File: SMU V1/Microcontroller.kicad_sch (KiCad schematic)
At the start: 0 parts

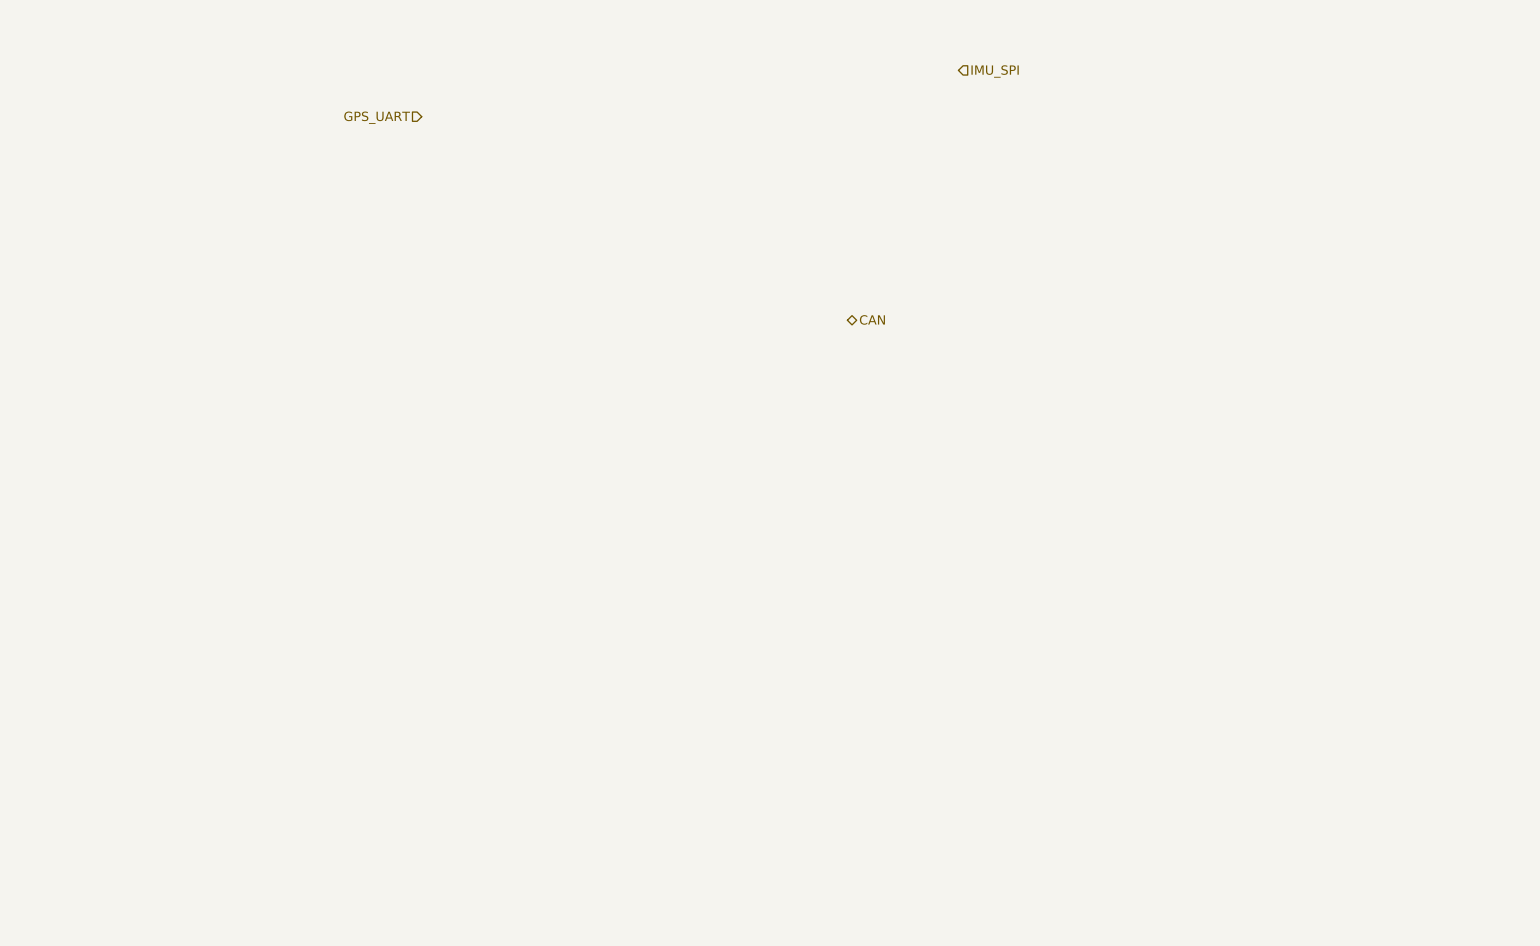
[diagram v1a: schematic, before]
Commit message: halfway done with routing, still needs antenna
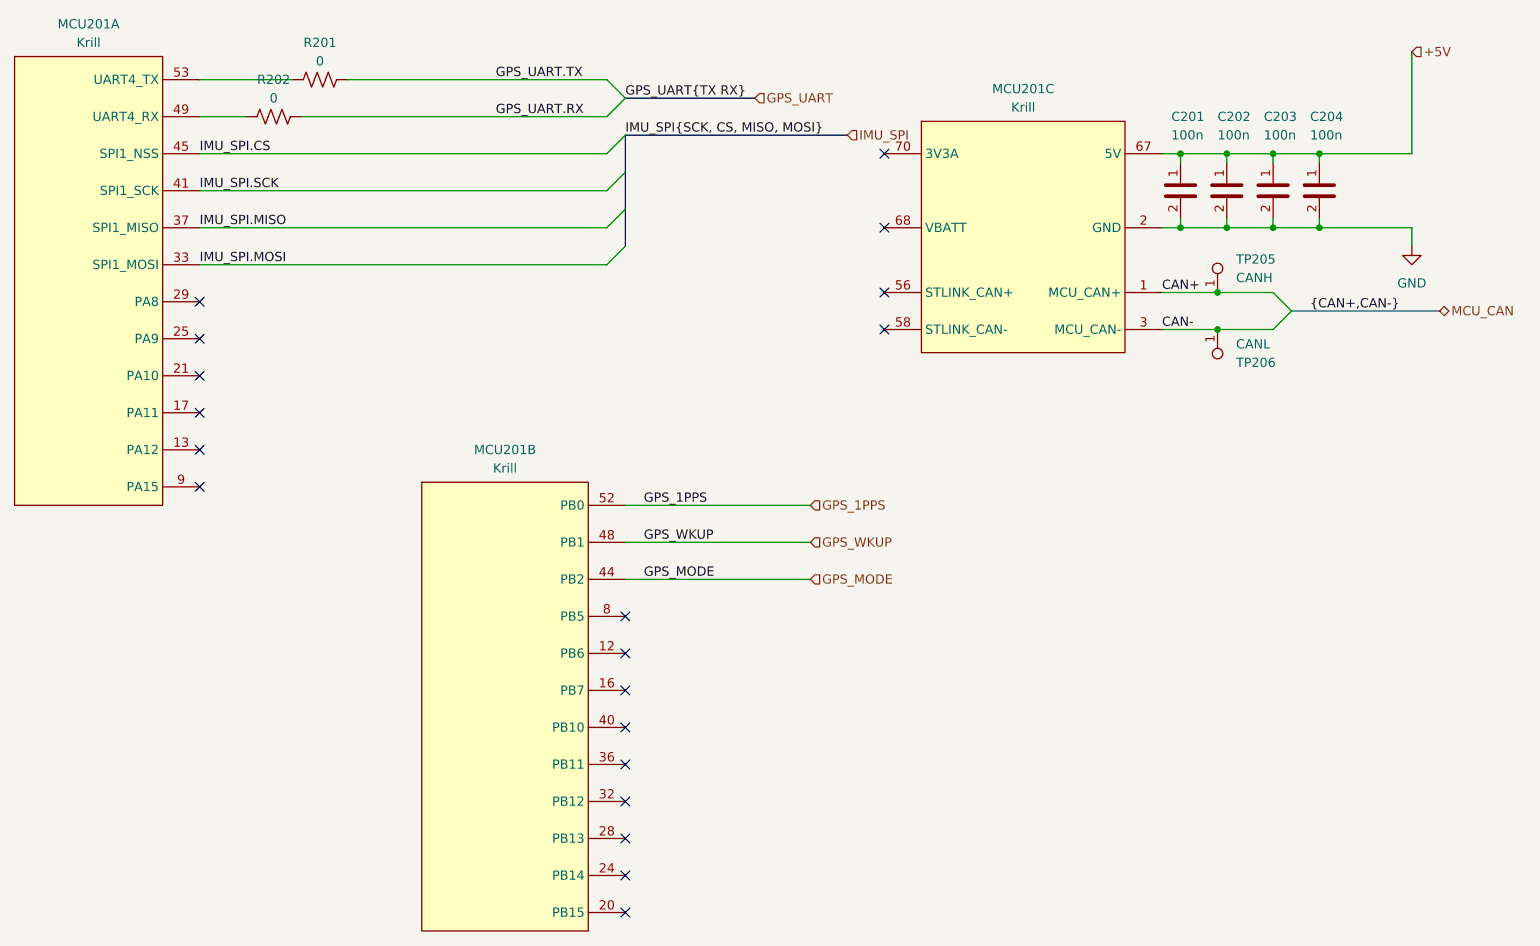
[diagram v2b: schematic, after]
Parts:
- added C201, C202, C203, C204: 100n, Capacitor_SMD:C_0402_1005Metric_Pad0.74x0.62mm_HandSolder, symbol bfr_capacitors:CL05B104KO5NNNC
- added MCU201: Krill, bfr_connectors:TE_1-2199119-5, symbol bfr_microcontrollers:Krill
- added R201, R202: 0, Resistor_SMD:R_0603_1608Metric_Pad0.98x0.95mm_HandSolder, symbol bfr_resistors:RMCF0603ZT0R00
- added TP205: CANH, bfr_utilities:TestPoint_Keystone_5019_Miniature, symbol bfr_utilities:SMD_Test_Point
- added TP206: CANL, bfr_utilities:TestPoint_Keystone_5019_Miniature, symbol bfr_utilities:SMD_Test_Point
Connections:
- new net: MCU201.49 (PA1), R202.1
- new net: MCU201.53 (PA0), R201.1
- new net: MCU201.70 (3V3A), MCU201.72 (3V3A), MCU201.74 (3V3A)
- new net +5V: C201.1, C202.1, C203.1, C204.1, MCU201.67 (5V), MCU201.69 (5V), MCU201.71 (5V)
- new net CAN+: MCU201.1 (MCU_CAN+), TP205.1
- new net CAN-: MCU201.3 (MCU_CAN-), TP206.1
- new net GND: C201.2, C202.2, C203.2, C204.2, MCU201.10 (GND), MCU201.11 (GND), MCU201.14 (GND), MCU201.15 (GND), MCU201.18 (GND), MCU201.19 (GND), MCU201.2 (GND), MCU201.22 (GND), MCU201.23 (GND), MCU201.26 (GND), MCU201.27 (GND), MCU201.30 (GND), MCU201.31 (GND), MCU201.34 (GND), MCU201.35 (GND), MCU201.38 (GND), MCU201.39 (GND), MCU201.4 (GND), MCU201.42 (GND), MCU201.43 (GND), MCU201.46 (GND), MCU201.47 (GND), MCU201.5 (GND), MCU201.50 (GND), MCU201.51 (GND), MCU201.54 (GND), MCU201.55 (GND), MCU201.57 (GND), MCU201.6 (GND), MCU201.7 (GND), MCU201.73 (GND), MCU201.75 (GND)
- new net GPS_1PPS: MCU201.52 (PB0)
- new net GPS_MODE: MCU201.44 (PB2)
- new net GPS_UART.RX: R202.2
- new net GPS_UART.TX: R201.2
- new net GPS_WKUP: MCU201.48 (PB1)
- new net IMU_SPI.CS: MCU201.45 (PA4)
- new net IMU_SPI.MISO: MCU201.37 (PA6)
- new net IMU_SPI.MOSI: MCU201.33 (PA7)
- new net IMU_SPI.SCK: MCU201.41 (PA5)
- no-connect marks 0 -> 19

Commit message: finished, should prob double check the high frequency stuff
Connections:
- net GPS_WKUP: no longer names the net of MCU201.48 (PB1)
- no-connect marks 19 -> 20
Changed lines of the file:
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@@
+	)
+	(no_connect
+		(at 115.57 135.89)
 	)
 	(no_connect
@@
 	(wire
 		(pts
-			(xy 115.57 135.89) (xy 140.97 135.89)
-		)
-		(stroke
-			(width 0)
-			(type default)
-		)
-	)
-	(wire
-		(pts
 			(xy 210.82 82.55) (xy 223.52 82.55)
 		)
@@
 		)
 	)
-	(label "GPS_WKUP"
-		(at 118.11 135.89 0)
-		(effects
-			(font
-				(size 1.27 1.27)
-			)
-			(justify left bottom)
-		)
-	)
-	(hierarchical_label "GPS_WKUP"
-		(shape input)
-		(at 140.97 135.89 0)
-		(effects
-			(font
-				(size 1.27 1.27)
-			)
-			(justify left)
-		)
-	)
